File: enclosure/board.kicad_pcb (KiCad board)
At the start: 2 copper layers, 81.3 x 40.3 mm, 10 parts, among them J1 61900411021, J3 2x7, J4 02x17, J5 629105150521, SW1 SW_DPDT_x2

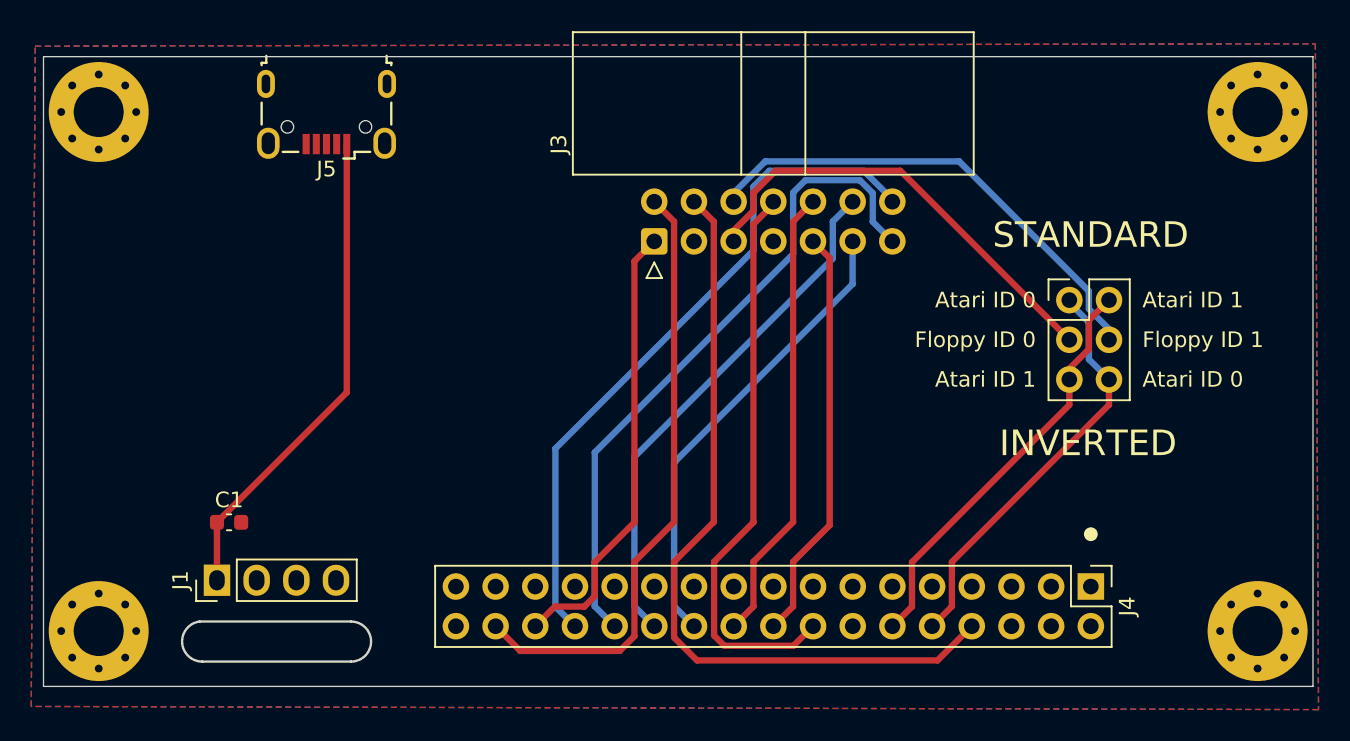
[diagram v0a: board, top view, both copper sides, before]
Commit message: Fix cap value, thicker text, and minor layout tweaks
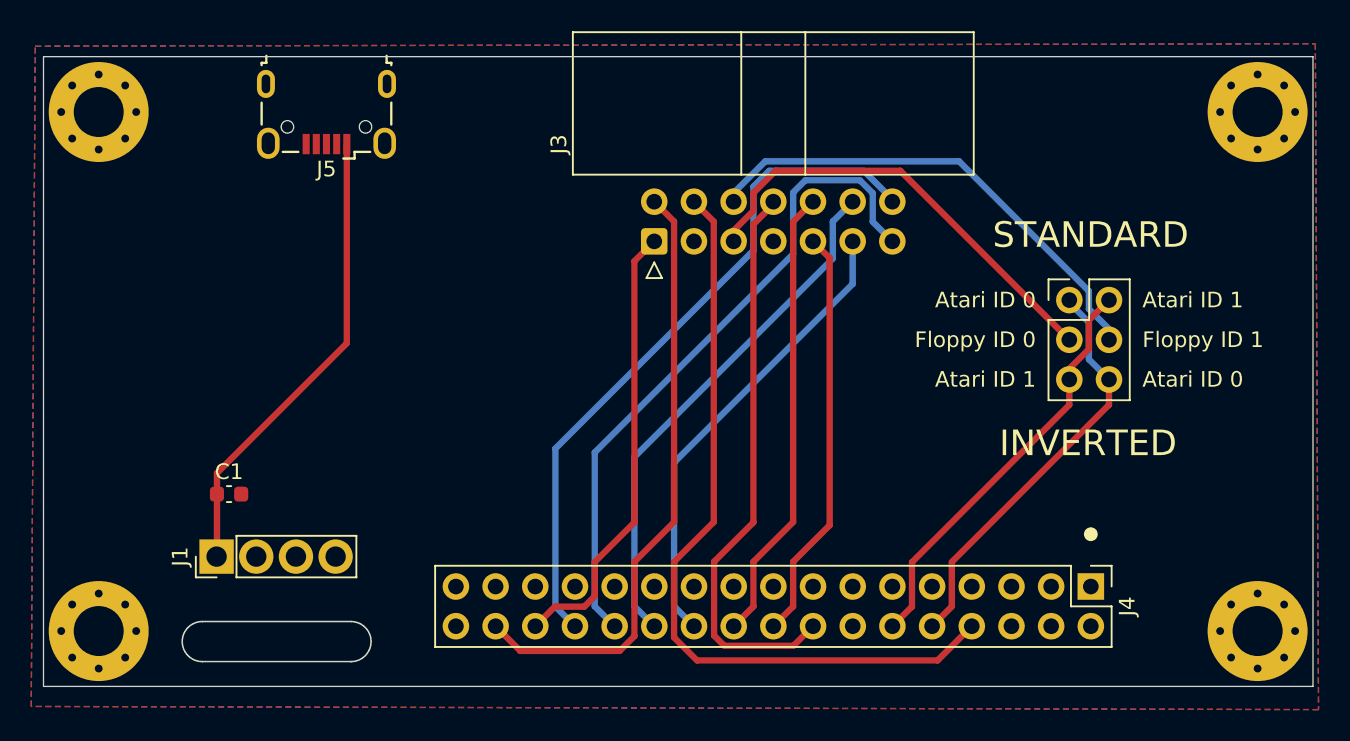
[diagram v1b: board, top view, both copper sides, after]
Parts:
- C1: value 1pF -> 2.2uF
- moved C1 1.81 mm to (119.7, 112.8)
- moved J1 1.51 mm to (119.0, 116.8)
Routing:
- net VCC: track 31.4 -> 29.9 mm
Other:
- outline, holes or cut-outs redrawn

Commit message: spacing tweaks
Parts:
- moved J1 5.12 mm to (118.3, 111.8)
- moved C1 5.12 mm to (119.1, 107.8)
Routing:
- net VCC: track 29.9 -> 25.0 mm
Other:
- outline, holes or cut-outs redrawn

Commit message: add info to board
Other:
- board text added: "Atari ST Floppy Adapter v1.0.2 https://5vsupply.com nick@5vsupply.com"
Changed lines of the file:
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@@
     (effects (font (size 1.63576 1.63576) (thickness 0.2)) (justify left bottom))
+  )
+  (gr_text "Atari ST Floppy Adapter v1.0.2\nhttps://5vsupply.com\nnick@5vsupply.com" (at 148.59 112.395) (layer "F.SilkS")
+    (effects (font (size 1.3 1.3) (thickness 0.2)))
   )
   (segment (start 118.3386 107.77) (end 127.284 98.8246) (width 0.4064) (layer "F.Cu") (net 2))
